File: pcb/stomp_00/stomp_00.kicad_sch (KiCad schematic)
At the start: 23 parts, among them J2 GuitarInput1, J2 GuitarOutput1, J5 Conn_01x09_Pin, SW1 SW_DIP_x04, SW2 Footswitch, U7 Teensy4.1

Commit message: pcb...
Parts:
- removed D5: LED, LED_THT:LED_D5.0mm, symbol Device:LED
- removed H3, H4: MountingHole, MountingHole:MountingHole_3.2mm_M3, symbol Mechanical:MountingHole
- removed J2: GuitarInput1, Connector_Audio:Jack_6.35mm_Neutrik_NMJ4HCD2_Horizontal, symbol Connector_Audio:NMJ4HCD2
- removed J2: GuitarOutput1, Connector_Audio:Jack_6.35mm_Neutrik_NMJ4HCD2_Horizontal, symbol Connector_Audio:NMJ4HCD2
- removed J5: Conn_01x09_Pin, Connector_PinHeader_2.54mm:PinHeader_1x09_P2.54mm_Vertical, symbol Connector:Conn_01x09_Pin
- removed JP1, JP2, JP3, JP4, JP6, JP7, JP8, JP9: Jumper_2_Bridged, Jumper:SolderJumper-2_P1.3mm_Bridged2Bar_RoundedPad1.0x1.5mm, symbol Jumper:Jumper_2_Bridged
- removed R16: R_US, Resistor_THT:R_Axial_DIN0207_L6.3mm_D2.5mm_P7.62mm_Horizontal, symbol Device:R_US
- removed RV4, RV5, RV6: R_Potentiometer_US, Potentiometer_THT:Potentiometer_Piher_PC-16_Single_Vertical, symbol Device:R_Potentiometer_US
- removed SW2: Footswitch, stomp:Footswitch_3PDT, symbol stomp:SW_3PDT
- added J7: Conn_02x04_Counter_Clockwise, Connector_PinHeader_2.54mm:PinHeader_2x04_P2.54mm_Vertical, symbol Connector_Generic:Conn_02x04_Counter_Clockwise
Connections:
- new net +3.3V: J7.5 (Pin_5), J7.6 (Pin_6), J7.7 (Pin_7), J7.8 (Pin_8)
- new net GND: J7.1 (Pin_1), J7.2 (Pin_2), J7.3 (Pin_3), J7.4 (Pin_4)
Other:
- added sheet Footswitch (footswitch.kicad_sch)

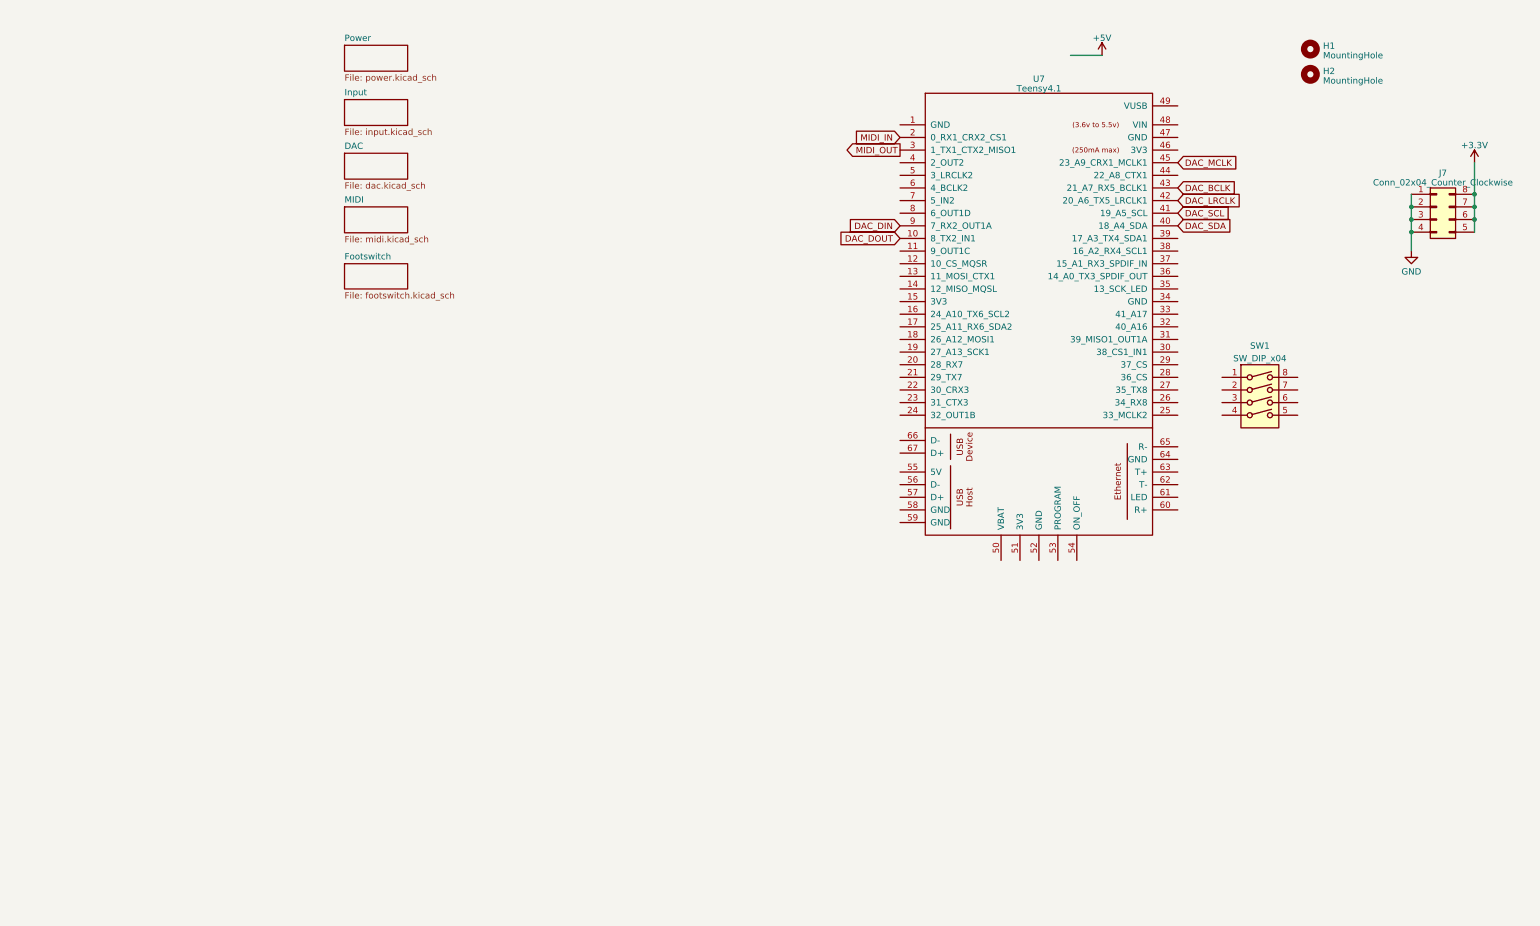
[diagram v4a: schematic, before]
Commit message: adding perfboard section
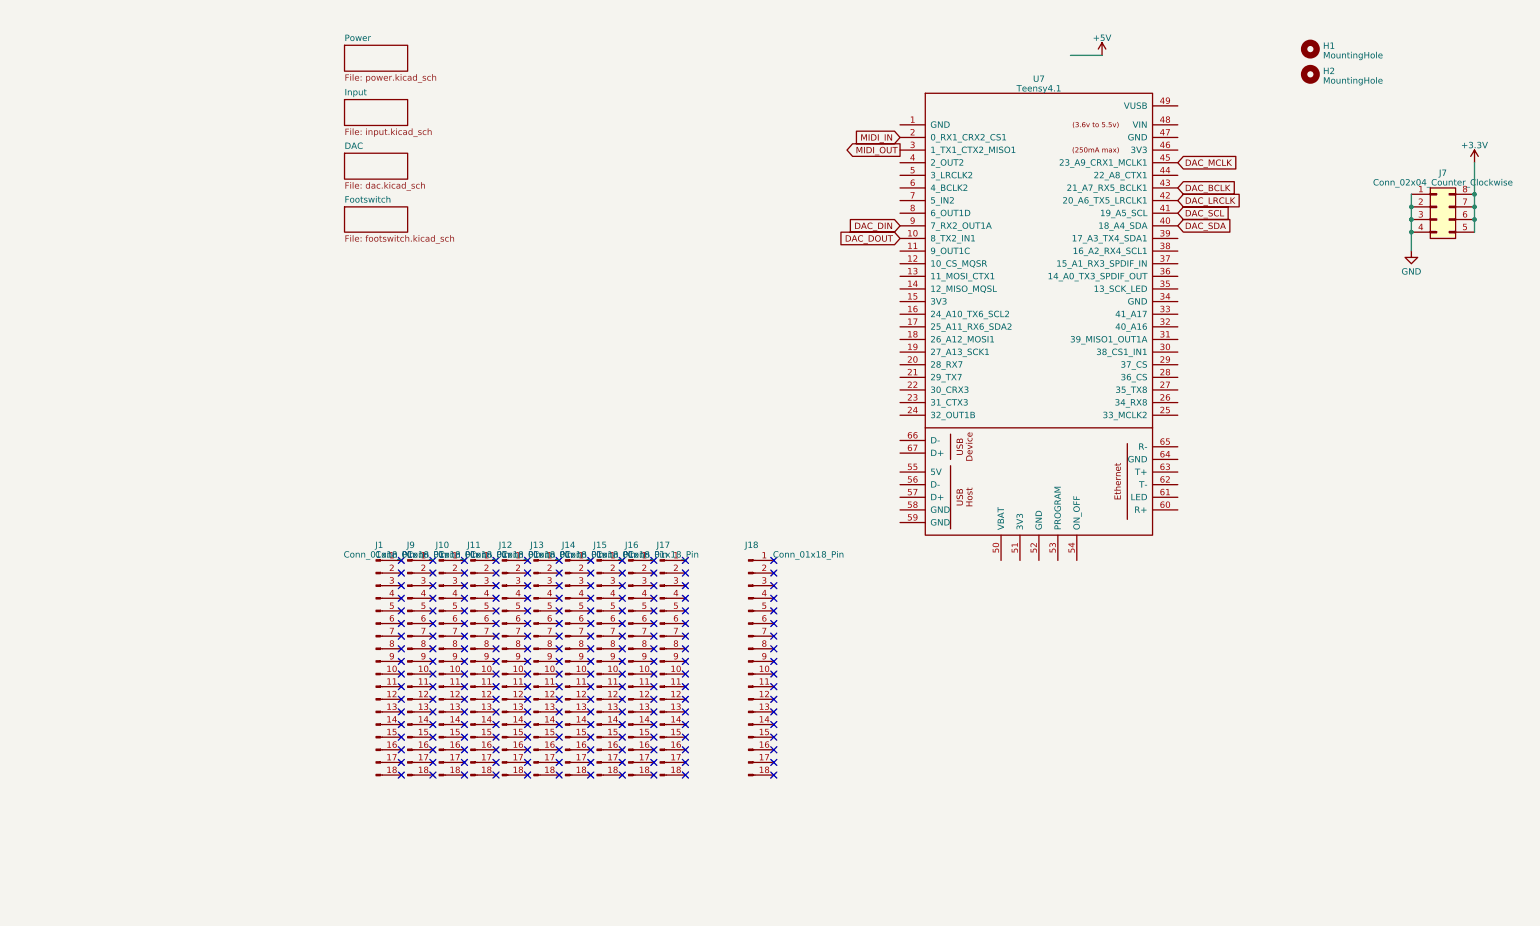
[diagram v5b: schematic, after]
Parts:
- removed SW1: SW_DIP_x04, Button_Switch_THT:SW_DIP_SPSTx04_Slide_9.78x12.34mm_W7.62mm_P2.54mm, symbol Switch:SW_DIP_x04
- added J1, J10, J11, J12, J13, J14, J15, J16, J17, J18, J9: Conn_01x18_Pin, Connector_PinHeader_2.54mm:PinHeader_1x18_P2.54mm_Vertical, symbol Connector:Conn_01x18_Pin
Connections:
- no-connect marks 0 -> 198
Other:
- removed sheet MIDI

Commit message: tidying up footprints, layout, etc
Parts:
- removed J1: Conn_01x18_Pin, Connector_PinHeader_2.54mm:PinHeader_1x18_P2.54mm_Vertical, symbol Connector:Conn_01x18_Pin
- removed J7: Conn_02x04_Counter_Clockwise, Connector_PinHeader_2.54mm:PinHeader_2x04_P2.54mm_Vertical, symbol Connector_Generic:Conn_02x04_Counter_Clockwise
- J10, J11, J12, J13, J14, J15, J16, J17, J18, J9: footprint Connector_PinHeader_2.54mm:PinHeader_1x18_P2.54mm_Vertical -> stomp:PinHeader_1x18_P2.54mm_Vertical_perf
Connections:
- net +3.3V: now also J9.1 (Pin_1), J9.2 (Pin_2), J9.3 (Pin_3)
- net GND: now also J9.16 (Pin_16), J9.17 (Pin_17), J9.18 (Pin_18)
- no-connect marks 198 -> 174

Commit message: not much
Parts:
- renumbered J9 to J1, J18 to J10, J10 to J2, J11 to J3, J12 to J4, J13 to J5, J14 to J6, J15 to J7, J16 to J8, J17 to J9, U7 to U1
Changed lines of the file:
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@@
   (symbol (lib_id "teensy:Teensy4.1") (at 160.02 95.25 0) (unit 1)
     (in_bom yes) (on_board yes) (dnp no) (fields_autoplaced)
-    (property "Reference" "U7" (at 160.02 31.4071 0)
+    (property "Reference" "U1" (at 160.02 31.4071 0)
       (effects (font (size 1.27 1.27)))
     )
@@
       (project "stomp_00"
         (path "/8f4a2eb0-078b-46cb-b534-a4acd11d130e"
-          (reference "U7") (unit 1)
+          (reference "U1") (unit 1)
         )
       )
@@
   (symbol (lib_id "Connector:Conn_01x18_Pin") (at 101.6 148.59 0) (unit 1)
     (in_bom yes) (on_board yes) (dnp no)
-    (property "Reference" "J18" (at 102.235 125.1839 0)
+    (property "Reference" "J10" (at 102.235 125.1839 0)
       (effects (font (size 1.27 1.27)))
     )
@@
       (project "stomp_00"
         (path "/8f4a2eb0-078b-46cb-b534-a4acd11d130e"
-          (reference "J18") (unit 1)
+          (reference "J10") (unit 1)
         )
       )
@@
   (symbol (lib_id "Connector:Conn_01x18_Pin") (at 33.02 148.59 0) (unit 1)
     (in_bom yes) (on_board yes) (dnp no) (fields_autoplaced)
-    (property "Reference" "J9" (at 33.655 125.1839 0)
+    (property "Reference" "J1" (at 33.655 125.1839 0)
       (effects (font (size 1.27 1.27)))
     )
@@
       (project "stomp_00"
         (path "/8f4a2eb0-078b-46cb-b534-a4acd11d130e"
+          (reference "J1") (unit 1)
+        )
+      )
+    )
+  )
+  (symbol (lib_id "Connector:Conn_01x18_Pin") (at 64.77 148.59 0) (unit 1)
+    (in_bom yes) (on_board yes) (dnp no) (fields_autoplaced)
+    (property "Reference" "J6" (at 65.405 125.1839 0)
+      (effects (font (size 1.27 1.27)))
+    )
+    (property "Value" "Conn_01x18_Pin" (at 65.405 127.1049 0)
+      (effects (font (size 1.27 1.27)))
+    )
+    (property "Footprint" "stomp:PinHeader_1x18_P2.54mm_Vertical_perf" (at 64.77 148.59 0)
+      (effects (font (size 1.27 1.27)) hide)
+    )
+    (property "Datasheet" "~" (at 64.77 148.59 0)
+      (effects (font (size 1.27 1.27)) hide)
+    )
+    (pin "1")
+    (pin "10")
+    (pin "11")
+    (pin "12")
+    (pin "13")
+    (pin "14")
+    (pin "15")
+    (pin "16")
+    (pin "17")
+    (pin "18")
+    (pin "2")
+    (pin "3")
+    (pin "4")
+    (pin "5")
+    (pin "6")
+    (pin "7")
+    (pin "8")
+    (pin "9")
+    (instances
+      (project "stomp_00"
+        (path "/8f4a2eb0-078b-46cb-b534-a4acd11d130e"
+          (reference "J6") (unit 1)
+        )
+      )
+    )
+  )
+  (symbol (lib_id "Connector:Conn_01x18_Pin") (at 83.82 148.59 0) (unit 1)
+    (in_bom yes) (on_board yes) (dnp no) (fields_autoplaced)
+    (property "Reference" "J9" (at 84.455 125.1839 0)
+      (effects (font (size 1.27 1.27)))
+    )
+    (property "Value" "Conn_01x18_Pin" (at 84.455 127.1049 0)
+      (effects (font (size 1.27 1.27)))
+    )
+    (property "Footprint" "stomp:PinHeader_1x18_P2.54mm_Vertical_perf" (at 83.82 148.59 0)
+      (effects (font (size 1.27 1.27)) hide)
+    )
+    (property "Datasheet" "~" (at 83.82 148.59 0)
+      (effects (font (size 1.27 1.27)) hide)
+    )
+    (pin "1")
+    (pin "10")
+    (pin "11")
+    (pin "12")
+    (pin "13")
+    (pin "14")
+    (pin "15")
+    (pin "16")
+    (pin "17")
+    (pin "18")
+    (pin "2")
+    (pin "3")
+    (pin "4")
+    (pin "5")
+    (pin "6")
+    (pin "7")
+    (pin "8")
+    (pin "9")
+    (instances
+      (project "stomp_00"
+        (path "/8f4a2eb0-078b-46cb-b534-a4acd11d130e"
           (reference "J9") (unit 1)
         )
@@
     )
   )
-  (symbol (lib_id "Connector:Conn_01x18_Pin") (at 64.77 148.59 0) (unit 1)
-    (in_bom yes) (on_board yes) (dnp no) (fields_autoplaced)
-    (property "Reference" "J14" (at 65.405 125.1839 0)
-      (effects (font (size 1.27 1.27)))
-    )
-    (property "Value" "Conn_01x18_Pin" (at 65.405 127.1049 0)
-      (effects (font (size 1.27 1.27)))
-    )
-    (property "Footprint" "stomp:PinHeader_1x18_P2.54mm_Vertical_perf" (at 64.77 148.59 0)
-      (effects (font (size 1.27 1.27)) hide)
-    )
-    (property "Datasheet" "~" (at 64.77 148.59 0)
-      (effects (font (size 1.27 1.27)) hide)
-    )
-    (pin "1")
-    (pin "10")
-    (pin "11")
-    (pin "12")
-    (pin "13")
-    (pin "14")
-    (pin "15")
-    (pin "16")
-    (pin "17")
-    (pin "18")
-    (pin "2")
-    (pin "3")
-    (pin "4")
-    (pin "5")
-    (pin "6")
-    (pin "7")
-    (pin "8")
-    (pin "9")
-    (instances
-      (project "stomp_00"
-        (path "/8f4a2eb0-078b-46cb-b534-a4acd11d130e"
-          (reference "J14") (unit 1)
-        )
-      )
-    )
-  )
-  (symbol (lib_id "Connector:Conn_01x18_Pin") (at 83.82 148.59 0) (unit 1)
-    (in_bom yes) (on_board yes) (dnp no) (fields_autoplaced)
-    (property "Reference" "J17" (at 84.455 125.1839 0)
-      (effects (font (size 1.27 1.27)))
-    )
-    (property "Value" "Conn_01x18_Pin" (at 84.455 127.1049 0)
-      (effects (font (size 1.27 1.27)))
-    )
-    (property "Footprint" "stomp:PinHeader_1x18_P2.54mm_Vertical_perf" (at 83.82 148.59 0)
-      (effects (font (size 1.27 1.27)) hide)
-    )
-    (property "Datasheet" "~" (at 83.82 148.59 0)
-      (effects (font (size 1.27 1.27)) hide)
-    )
-    (pin "1")
-    (pin "10")
-    (pin "11")
-    (pin "12")
-    (pin "13")
-    (pin "14")
-    (pin "15")
-    (pin "16")
-    (pin "17")
-    (pin "18")
-    (pin "2")
-    (pin "3")
-    (pin "4")
-    (pin "5")
-    (pin "6")
-    (pin "7")
-    (pin "8")
-    (pin "9")
-    (instances
-      (project "stomp_00"
-        (path "/8f4a2eb0-078b-46cb-b534-a4acd11d130e"
-          (reference "J17") (unit 1)
-        )
-      )
-    )
-  )
   (symbol (lib_id "Connector:Conn_01x18_Pin") (at 45.72 148.59 0) (unit 1)
     (in_bom yes) (on_board yes) (dnp no) (fields_autoplaced)
-    (property "Reference" "J11" (at 46.355 125.1839 0)
+    (property "Reference" "J3" (at 46.355 125.1839 0)
       (effects (font (size 1.27 1.27)))
     )
@@
       (project "stomp_00"
         (path "/8f4a2eb0-078b-46cb-b534-a4acd11d130e"
-          (reference "J11") (unit 1)
+          (reference "J3") (unit 1)
         )
       )
@@
   (symbol (lib_id "power:+3.3V") (at 38.1 123.19 0) (unit 1)
     (in_bom yes) (on_board yes) (dnp no) (fields_autoplaced)
-    (property "Reference" "#PWR07" (at 38.1 127 0)
+    (property "Reference" "#PWR01" (at 38.1 127 0)
       (effects (font (size 1.27 1.27)) hide)
     )
@@
       (project "stomp_00"
         (path "/8f4a2eb0-078b-46cb-b534-a4acd11d130e"
-          (reference "#PWR07") (unit 1)
+          (reference "#PWR01") (unit 1)
         )
       )
@@
   (symbol (lib_id "Connector:Conn_01x18_Pin") (at 71.12 148.59 0) (unit 1)
     (in_bom yes) (on_board yes) (dnp no) (fields_autoplaced)
-    (property "Reference" "J15" (at 71.755 125.1839 0)
+    (property "Reference" "J7" (at 71.755 125.1839 0)
       (effects (font (size 1.27 1.27)))
     )
@@
       (project "stomp_00"
         (path "/8f4a2eb0-078b-46cb-b534-a4acd11d130e"
-          (reference "J15") (unit 1)
+          (reference "J7") (unit 1)
         )
       )
@@
   (symbol (lib_id "Connector:Conn_01x18_Pin") (at 77.47 148.59 0) (unit 1)
     (in_bom yes) (on_board yes) (dnp no) (fields_autoplaced)
-    (property "Reference" "J16" (at 78.105 125.1839 0)
+    (property "Reference" "J8" (at 78.105 125.1839 0)
       (effects (font (size 1.27 1.27)))
     )
@@
       (project "stomp_00"
         (path "/8f4a2eb0-078b-46cb-b534-a4acd11d130e"
-          (reference "J16") (unit 1)
+          (reference "J8") (unit 1)
         )
       )
@@
   (symbol (lib_id "Connector:Conn_01x18_Pin") (at 58.42 148.59 0) (unit 1)
     (in_bom yes) (on_board yes) (dnp no) (fields_autoplaced)
-    (property "Reference" "J13" (at 59.055 125.1839 0)
+    (property "Reference" "J5" (at 59.055 125.1839 0)
       (effects (font (size 1.27 1.27)))
     )
@@
       (project "stomp_00"
         (path "/8f4a2eb0-078b-46cb-b534-a4acd11d130e"
-          (reference "J13") (unit 1)
+          (reference "J5") (unit 1)
         )
       )
@@
   (symbol (lib_id "Connector:Conn_01x18_Pin") (at 39.37 148.59 0) (unit 1)
     (in_bom yes) (on_board yes) (dnp no) (fields_autoplaced)
-    (property "Reference" "J10" (at 40.005 125.1839 0)
+    (property "Reference" "J2" (at 40.005 125.1839 0)
       (effects (font (size 1.27 1.27)))
     )
@@
       (project "stomp_00"
         (path "/8f4a2eb0-078b-46cb-b534-a4acd11d130e"
-          (reference "J10") (unit 1)
+          (reference "J2") (unit 1)
         )
       )
@@
       (project "stomp_00"
         (path "/8f4a2eb0-078b-46cb-b534-a4acd11d130e"
-          (reference "#PWR09") (unit 1)
+          (reference "#PWR03") (unit 1)
         )
         (path "/8f4a2eb0-078b-46cb-b534-a4acd11d130e/72df8ca6-692f-47f3-a8bd-ce94f6cd776a"
@@
   (symbol (lib_id "Connector:Conn_01x18_Pin") (at 52.07 148.59 0) (unit 1)
     (in_bom yes) (on_board yes) (dnp no) (fields_autoplaced)
-    (property "Reference" "J12" (at 52.705 125.1839 0)
+    (property "Reference" "J4" (at 52.705 125.1839 0)
       (effects (font (size 1.27 1.27)))
     )
@@
       (project "stomp_00"
         (path "/8f4a2eb0-078b-46cb-b534-a4acd11d130e"
-          (reference "J12") (unit 1)
+          (reference "J4") (unit 1)
         )
       )
@@
   (symbol (lib_id "power:GND") (at 38.1 173.99 0) (unit 1)
     (in_bom yes) (on_board yes) (dnp no) (fields_autoplaced)
-    (property "Reference" "#PWR04" (at 38.1 180.34 0)
+    (property "Reference" "#PWR02" (at 38.1 180.34 0)
       (effects (font (size 1.27 1.27)) hide)
     )
@@
       (project "stomp_00"
         (path "/8f4a2eb0-078b-46cb-b534-a4acd11d130e"
-          (reference "#PWR04") (unit 1)
-        )
-      )
+          (reference "#PWR02") (unit 1)
+        )
+      )

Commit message: layout getting closer
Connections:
- net +3.3V: now also J1.4 (Pin_4), J1.5 (Pin_5); no longer J1.1 (Pin_1), J1.2 (Pin_2)
- net GND: now also J1.15 (Pin_15)
- net LINE_IN_L: now reaches J1.10 (Pin_10)
- net LINE_IN_R: now reaches J1.11 (Pin_11)
- net LINE_OUT_L: now reaches J1.12 (Pin_12)
- net LINE_OUT_R: now reaches J1.13 (Pin_13)
- net LED_NEG: now reaches J1.14 (Pin_14)
- net JACK_IN: now reaches J1.6 (Pin_6)
- net JACK_OUT: now reaches J1.7 (Pin_7)
- net PREAMP_IN_L: now reaches J1.8 (Pin_8)
- net PREAMP_IN_R: now reaches J1.9 (Pin_9)
- new net +9V: J1.1 (Pin_1), J1.2 (Pin_2)
- no-connect marks 174 -> 162
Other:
- moved on the sheet: J1, J2, J3, J4, J5, J6, J7, J8, J9
